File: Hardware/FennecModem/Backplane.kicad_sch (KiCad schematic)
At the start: 28 parts, among them J1 SEL_ADDR, J3 EN_ADDR, J4 CARD_EN_BYPASS, Q901 MMBT3904, U2 SN74CBTLV3245A, U9 LM2596S-5

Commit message: Implement suggestions from KA2
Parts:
- removed JP1: SolderJumper_2_Open, Jumper:SolderJumper-2_P1.3mm_Open_TrianglePad1.0x1.5mm, symbol Jumper:SolderJumper_2_Open
- removed Q901: MMBT3904, Package_TO_SOT_SMD:SOT-23, symbol Transistor_BJT:MMBT3904
- removed R12: 0R, Resistor_SMD:R_0805_2012Metric, symbol Device:R_Small
- removed R13: 1k, Resistor_SMD:R_0805_2012Metric, symbol Device:R_Small
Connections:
- net +5VP: no longer R10.1
- net CARD_EN: now also R10.1
- net GND: now also R11.1; no longer R11.2
- net at R10.2, U2.19 (OE): now also R11.2; no longer R11.1
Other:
- note added: "CARD_EN, LOW = EN divider -> 3.3v"
- note removed: "5VP Always has power divider -> 3.3v pull low when EN high"
- note removed: "Solder this bypass and DNP inverter driver if CARD_EN is HIGH for disable"
- moved on the sheet: R10, R11

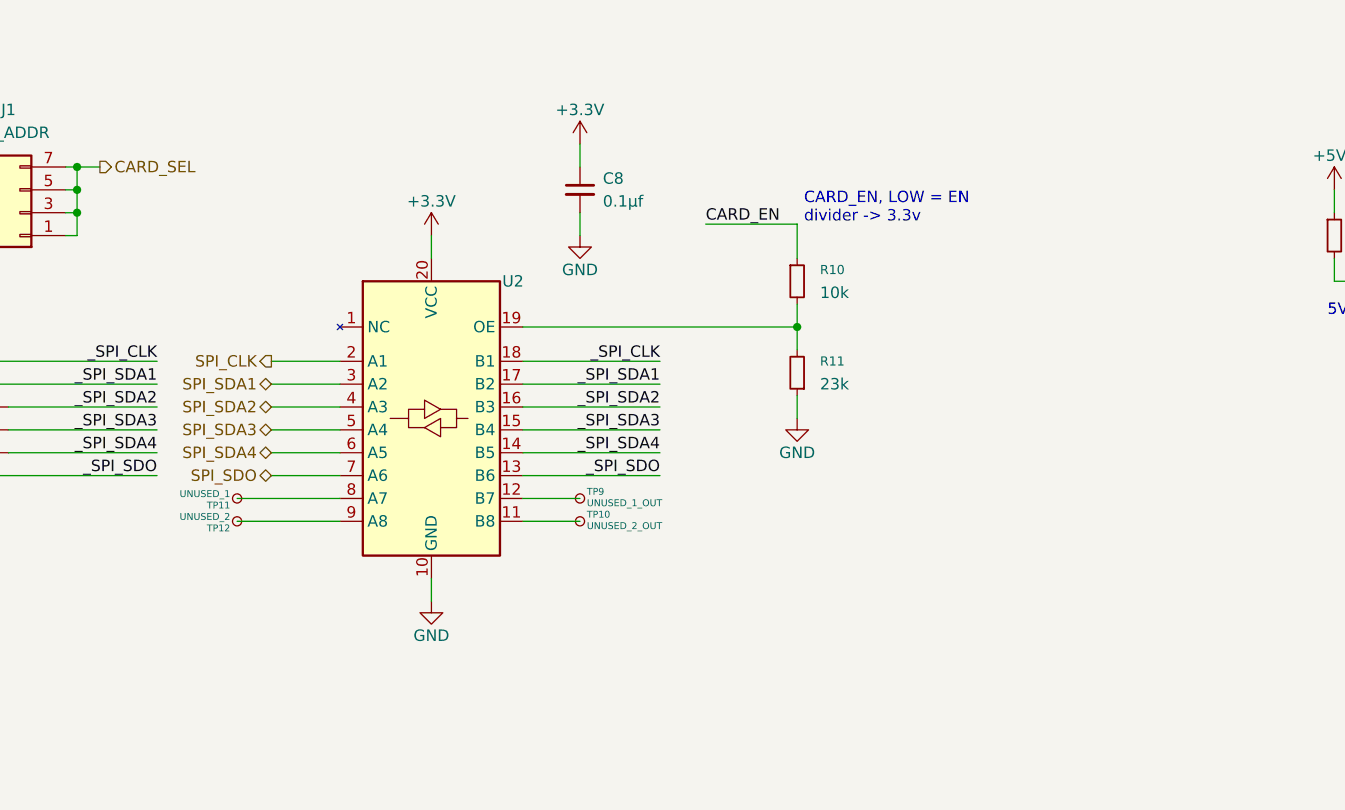
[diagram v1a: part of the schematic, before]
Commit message: Fix bom generation
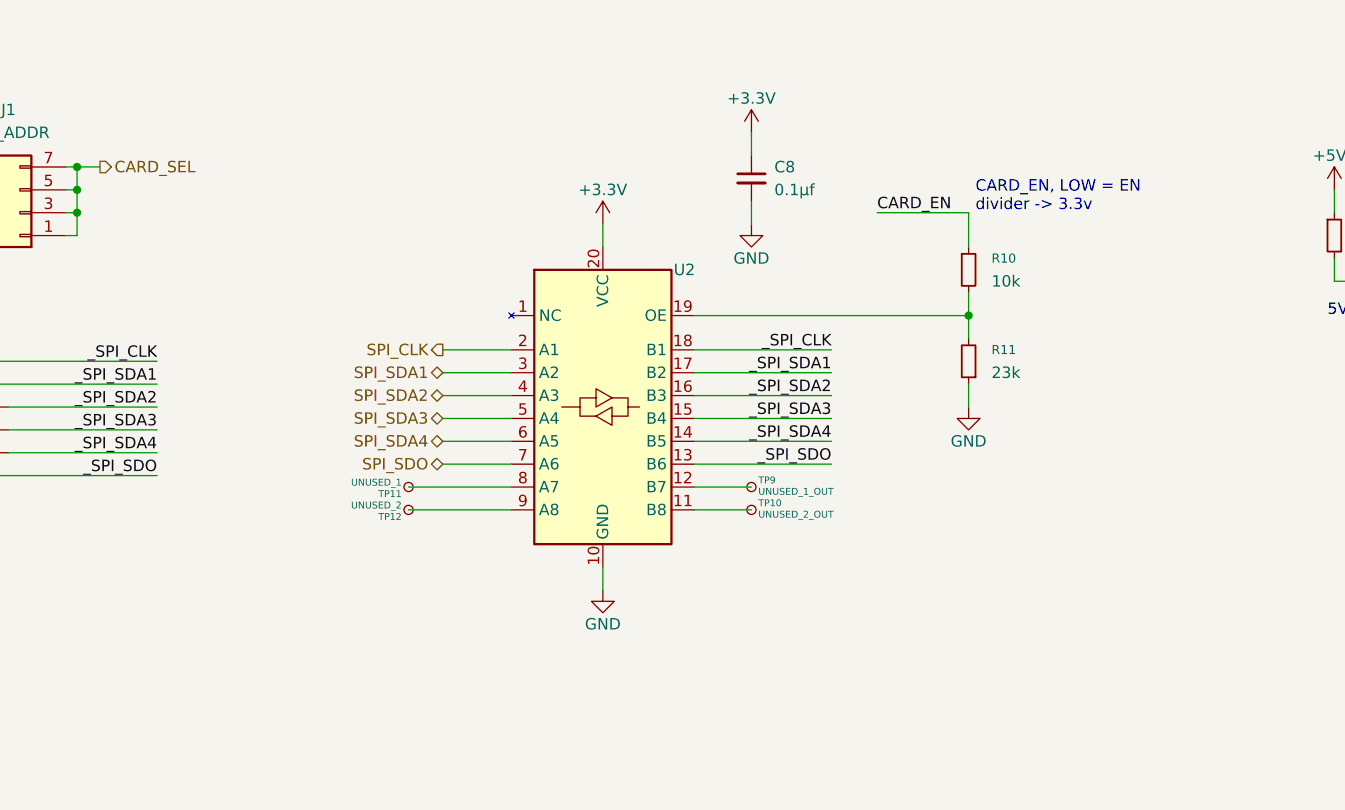
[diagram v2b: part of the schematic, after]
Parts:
- D1: LCSC C5295406 -> (none); LCSC# (none) -> C5295406
- U2: LCSC C2878923 -> (none); LCSC# (none) -> C2878923
- U9: LCSC C116713 -> (none); LCSC# (none) -> C116713
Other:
- moved on the sheet: C8, R10, R11, TP10, TP11, TP12, TP9, U2
